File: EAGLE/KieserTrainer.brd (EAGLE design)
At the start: 36.5 x 58.4 mm, 13 parts, among them U1 ATMEGA328P-PU

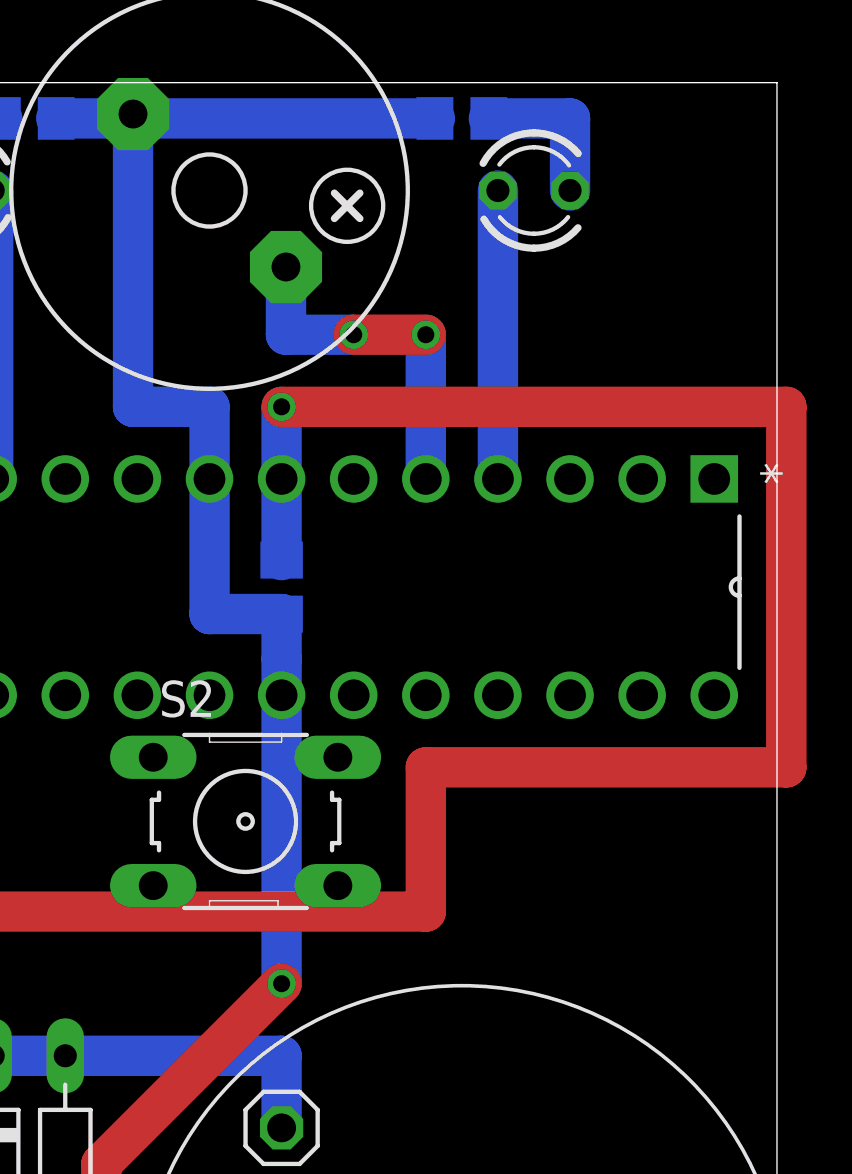
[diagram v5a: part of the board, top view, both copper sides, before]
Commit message: Add been/no beep feature, implement hardware interrupt for waking, rewire push button and LED
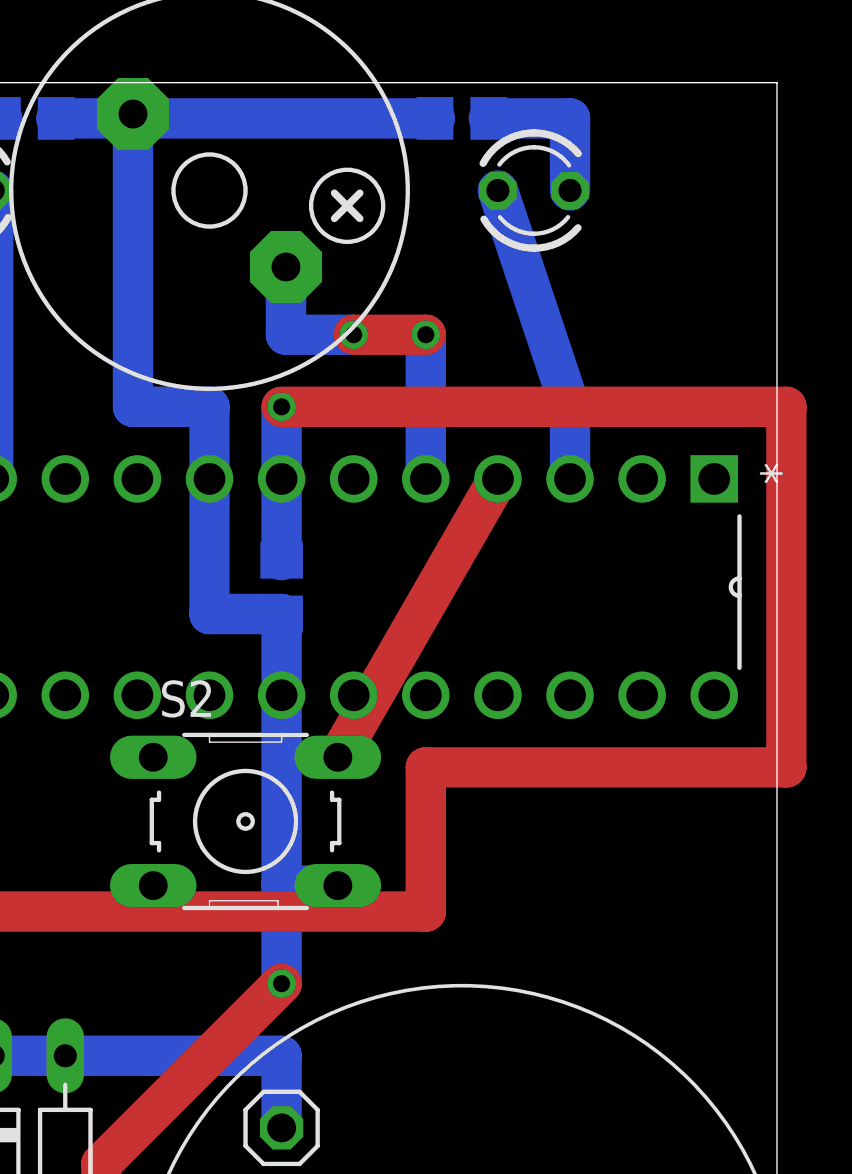
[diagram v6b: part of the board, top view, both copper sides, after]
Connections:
- new net N$7: S2.2, U1.4
- net GND: now also S2.4
- net N$3: now also U1.3; no longer U1.4
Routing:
- net N$7: track 0.00 -> 11.3 mm
- net GND: track 99.9 -> 101.9 mm
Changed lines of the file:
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@@
 <setting verticaltext="up"/>
 </settings>
-<grid distance="0.1" unitdist="inch" unit="inch" style="lines" multiple="1" display="no" altdistance="0.025" altunitdist="inch" altunit="inch"/>
+<grid distance="0.1" unitdist="inch" unit="inch" style="lines" multiple="1" display="no" altdistance="0.05" altunitdist="inch" altunit="inch"/>
 <layers>
 <layer number="1" name="Top" color="4" fill="1" visible="yes" active="yes"/>
@@
 <wire x1="24.45" y1="57.15" x2="13.815921875" y2="57.15" width="1.4224" layer="16"/>
 <wire x1="13.815921875" y1="57.15" x2="13.815921875" y2="57.304075" width="1.4224" layer="16"/>
-<wire x1="19.05" y1="36.83" x2="19.05" y2="38.1" width="1.4224" layer="16"/>
-<wire x1="19.05" y1="38.1" x2="19.05" y2="39.69" width="1.4224" layer="16"/>
+<wire x1="19.05" y1="36.83" x2="19.05" y2="39.69" width="1.4224" layer="16"/>
 <wire x1="19.05" y1="39.69" x2="16.51" y2="39.69" width="1.4224" layer="16"/>
 <wire x1="16.51" y1="39.69" x2="16.51" y2="44.45" width="1.4224" layer="16"/>
@@
 <wire x1="12.7" y1="20.32" x2="19.05" y2="26.67" width="1.4224" layer="1"/>
 <via x="19.05" y="26.67" extent="1-16" drill="0.6" shape="square"/>
-<wire x1="19.05" y1="26.67" x2="19.05" y2="36.83" width="1.4224" layer="16"/>
+<wire x1="19.05" y1="30.1244" x2="19.05" y2="36.83" width="1.4224" layer="16"/>
+<wire x1="19.05" y1="26.67" x2="19.05" y2="30.1244" width="1.4224" layer="16"/>
+<contactref element="S2" pad="4"/>
+<wire x1="19.05" y1="30.1244" x2="21.0312" y2="30.1244" width="1.4224" layer="16"/>
 </signal>
 <signal name="VCC">
@@
 <wire x1="8.89" y1="16.51" x2="11.43" y2="16.51" width="1.4224" layer="16"/>
 </signal>
-<signal name="N$3">
-<contactref element="U1" pad="4"/>
-<contactref element="LED1" pad="A"/>
-<wire x1="26.67" y1="44.45" x2="26.67" y2="54.61" width="1.4224" layer="16"/>
-</signal>
 <signal name="N$4">
 <contactref element="U1" pad="11"/>
@@
 <wire x1="11.43" y1="24.13" x2="8.89" y2="24.13" width="1.4224" layer="16"/>
 </signal>
+<signal name="N$3">
+<contactref element="LED1" pad="A"/>
+<contactref element="U1" pad="3"/>
+<wire x1="26.67" y1="54.61" x2="29.21" y2="46.99" width="1.4224" layer="16"/>
+<wire x1="29.21" y1="46.99" x2="29.21" y2="44.45" width="1.4224" layer="16"/>
+</signal>
+<signal name="N$7">
+<contactref element="U1" pad="4"/>
+<contactref element="S2" pad="2"/>
+<wire x1="26.67" y1="44.45" x2="21.0312" y2="34.6456" width="1.4224" layer="1"/>
+</signal>
 </signals>
